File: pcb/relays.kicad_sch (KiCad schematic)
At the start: 30 parts

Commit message: Upgrade kicad version to 10, add krita capacitor image
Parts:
- D6, D7, D8, H6, H7, H8, Q2, Q3, Q4, RLY1, RLY2, RLY3, U2: value ~ -> (none)

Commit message: Add JLC carts and BOM
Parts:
- C1, C2: Manufacturer Part (none) -> CL10A106KP8NNNC; Supplier (none) -> LCSC; Supplier Part URL (none) -> https://www.lcsc.com/product-detail/C19702.html
- D10, D11, D12: Manufacturer Part (none) -> YLED0603R; Supplier (none) -> LCSC; Supplier Part (none) -> C19171390; Supplier Part URL (none) -> https://www.lcsc.com/product-detail/C19171390.html
- D6, D7, D8: Supplier Part URL (none) -> https://www.lcsc.com/product-detail/C82544.html
- H6, H7, H8: Supplier Part URL (none) -> https://www.lcsc.com/product-detail/C7499322.html
- Q2, Q3, Q4: Supplier Part URL (none) -> https://www.lcsc.com/product-detail/C52801.html
- R10, R13, R16, R30, R31, R32: Manufacturer Part (none) -> RC0603FR-071KL; Supplier (none) -> LCSC; Supplier Part URL (none) -> https://www.lcsc.com/product-detail/C22548.html
- R11, R14, R17: Manufacturer Part (none) -> RC0603FR-0710KL; Supplier (none) -> LCSC; Supplier Part URL (none) -> https://www.lcsc.com/product-detail/C98220.html
- R12, R15, R18: Manufacturer Part (none) -> KNP3WS-10Ω±5% T; Supplier (none) -> LCSC; Supplier Part (none) -> C122149; Supplier Part URL (none) -> https://www.lcsc.com/product-detail/C122149.html
- RLY1, RLY2, RLY3: Supplier Part URL (none) -> https://www.lcsc.com/product-detail/C225714.html
- U2: Supplier Part URL (none) -> https://www.lcsc.com/product-detail/C45359464.html

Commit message: Update 10u capacitor to 25v rated one
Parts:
- C1, C2: Manufacturer Part CL10A106KP8NNNC -> CL10A106MA8NRNC; Supplier Part C19702 -> C96446; Supplier Part URL https://www.lcsc.com/product-detail/C19702.html -> https://www.lcsc.com/product-detail/C96446.html
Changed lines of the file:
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@@
 			)
 		)
-		(property "Supplier Part" "C19702"
+		(property "Supplier Part" "C96446"
 			(at 72.39 58.42 0)
 			(hide yes)
@@
 			)
 		)
-		(property "Manufacturer Part" "CL10A106KP8NNNC"
+		(property "Manufacturer Part" "CL10A106MA8NRNC"
 			(at 72.39 58.42 0)
 			(hide yes)
@@
 			)
 		)
-		(property "Supplier Part URL" "https://www.lcsc.com/product-detail/C19702.html"
+		(property "Supplier Part URL" "https://www.lcsc.com/product-detail/C96446.html"
 			(at 72.39 58.42 0)
 			(hide yes)
@@
 			)
 		)
-		(property "Supplier Part" "C19702"
+		(property "Supplier Part" "C96446"
 			(at 36.83 57.15 0)
 			(hide yes)
@@
 			)
 		)
-		(property "Manufacturer Part" "CL10A106KP8NNNC"
+		(property "Manufacturer Part" "CL10A106MA8NRNC"
 			(at 36.83 57.15 0)
 			(hide yes)
@@
 			)
 		)
-		(property "Supplier Part URL" "https://www.lcsc.com/product-detail/C19702.html"
+		(property "Supplier Part URL" "https://www.lcsc.com/product-detail/C96446.html"
 			(at 36.83 57.15 0)
 			(hide yes)

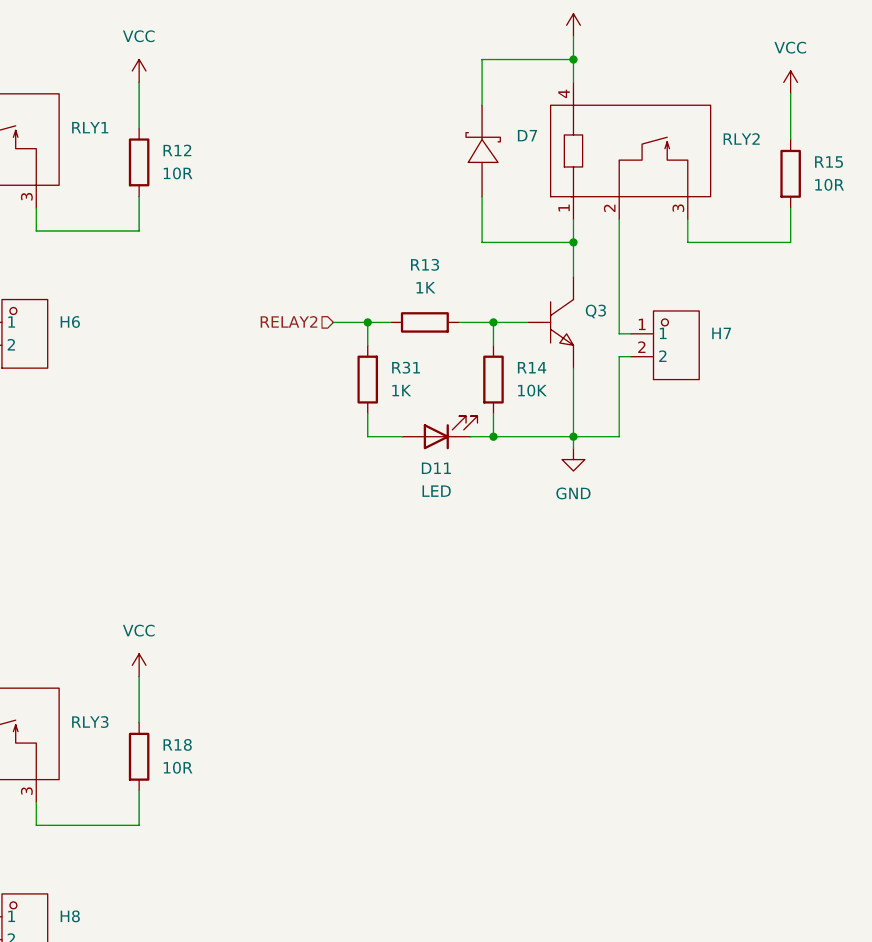
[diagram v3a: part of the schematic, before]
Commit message: Change input voltage range
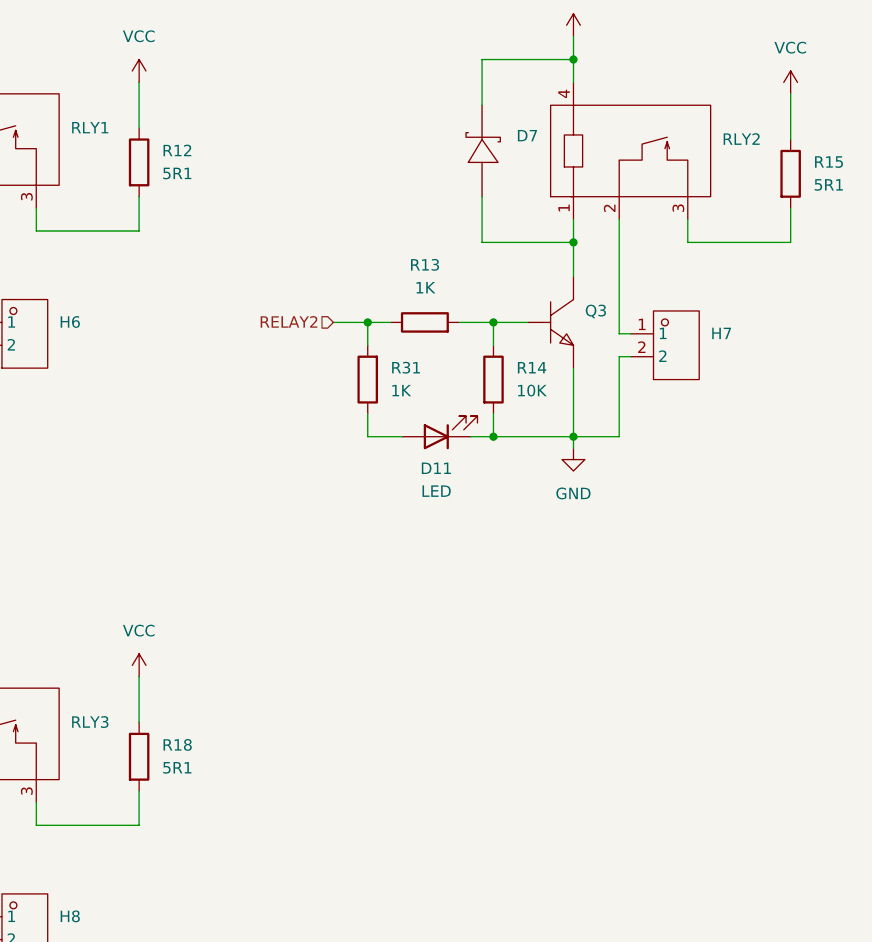
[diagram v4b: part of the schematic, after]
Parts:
- R12, R15, R18: value 10R -> 5R1; Manufacturer Part KNP3WS-10Ω±5% T -> MOF3WS-5.1Ω±5% T; Supplier Part C122149 -> C121777; Supplier Part URL https://www.lcsc.com/product-detail/C122149.html -> https://www.lcsc.com/product-detail/C121777.html
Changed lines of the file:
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@@
 			)
 		)
-		(property "Value" "10R"
+		(property "Value" "5R1"
 			(at 157.48 110.4899 0)
 			(show_name no)
@@
 			)
 		)
-		(property "Manufacturer Part" "KNP3WS-10Ω±5% T"
+		(property "Manufacturer Part" "MOF3WS-5.1Ω±5% T"
 			(at 154.94 109.22 0)
 			(hide yes)
@@
 			)
 		)
-		(property "Supplier Part" "C122149"
+		(property "Supplier Part" "C121777"
 			(at 154.94 109.22 0)
 			(hide yes)
@@
 			)
 		)
-		(property "Supplier Part URL" "https://www.lcsc.com/product-detail/C122149.html"
+		(property "Supplier Part URL" "https://www.lcsc.com/product-detail/C121777.html"
 			(at 154.94 109.22 0)
 			(hide yes)
@@
 			)
 		)
-		(property "Value" "10R"
+		(property "Value" "5R1"
 			(at 157.48 44.4499 0)
 			(show_name no)
@@
 			)
 		)
-		(property "Manufacturer Part" "KNP3WS-10Ω±5% T"
+		(property "Manufacturer Part" "MOF3WS-5.1Ω±5% T"
 			(at 154.94 43.18 0)
 			(hide yes)
@@
 			)
 		)
-		(property "Supplier Part" "C122149"
+		(property "Supplier Part" "C121777"
 			(at 154.94 43.18 0)
 			(hide yes)
@@
 			)
 		)
-		(property "Supplier Part URL" "https://www.lcsc.com/product-detail/C122149.html"
+		(property "Supplier Part URL" "https://www.lcsc.com/product-detail/C121777.html"
 			(at 154.94 43.18 0)
 			(hide yes)
@@
 			)
 		)
-		(property "Value" "10R"
+		(property "Value" "5R1"
 			(at 229.87 45.7199 0)
 			(show_name no)
@@
 			)
 		)
-		(property "Manufacturer Part" "KNP3WS-10Ω±5% T"
+		(property "Manufacturer Part" "MOF3WS-5.1Ω±5% T"
 			(at 227.33 44.45 0)
 			(hide yes)
@@
 			)
 		)
-		(property "Supplier Part" "C122149"
+		(property "Supplier Part" "C121777"
 			(at 227.33 44.45 0)
 			(hide yes)
@@
 			)
 		)
-		(property "Supplier Part URL" "https://www.lcsc.com/product-detail/C122149.html"
+		(property "Supplier Part URL" "https://www.lcsc.com/product-detail/C121777.html"
 			(at 227.33 44.45 0)
 			(hide yes)
